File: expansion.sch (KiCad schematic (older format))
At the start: 3 parts, among them J7 DF40HC(3.5)-60DS, J9 DF40HC(3.5)-60DS, U1 IMX8MM

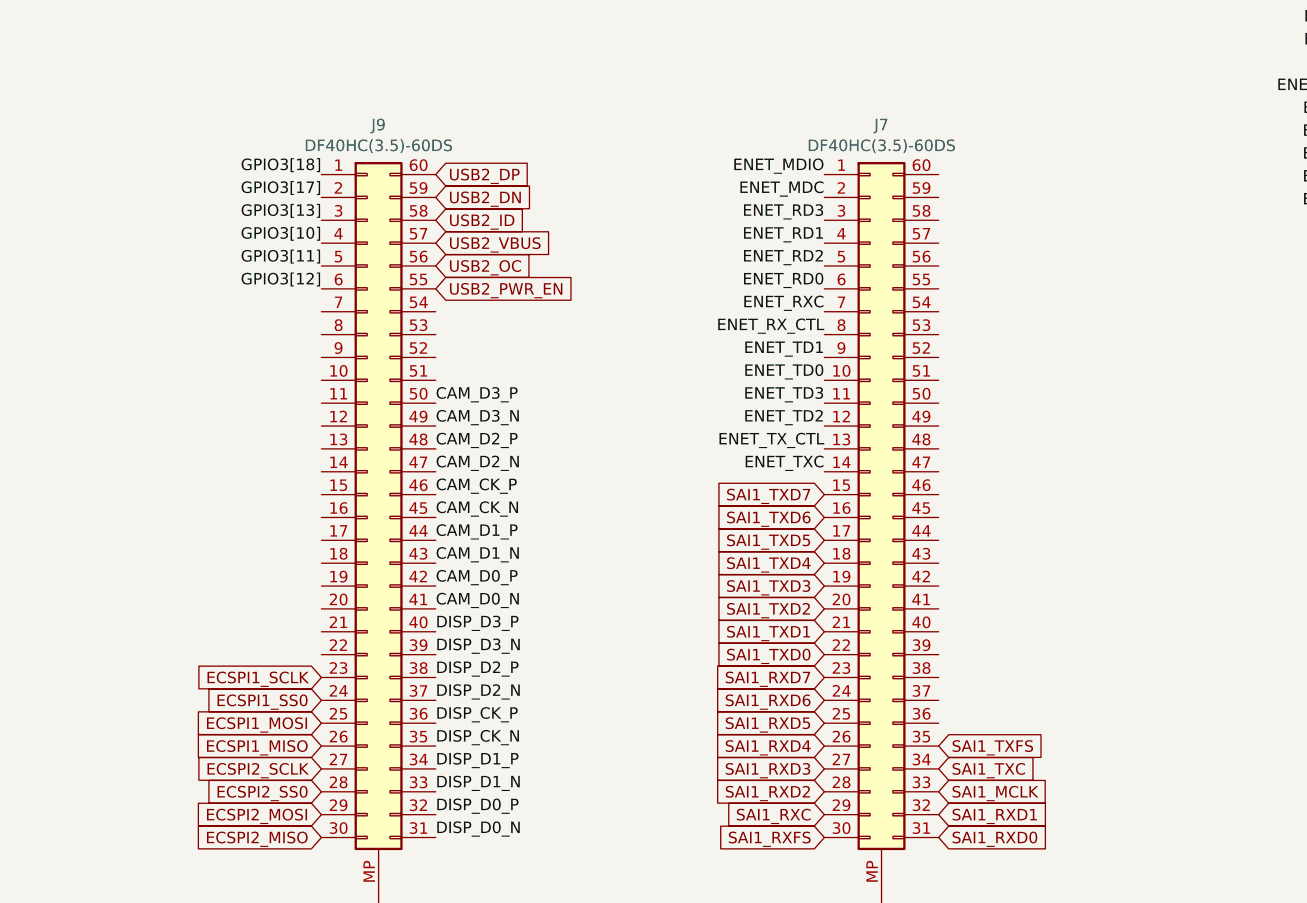
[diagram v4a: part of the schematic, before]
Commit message: UIM and USB routing for PCIE to expansion
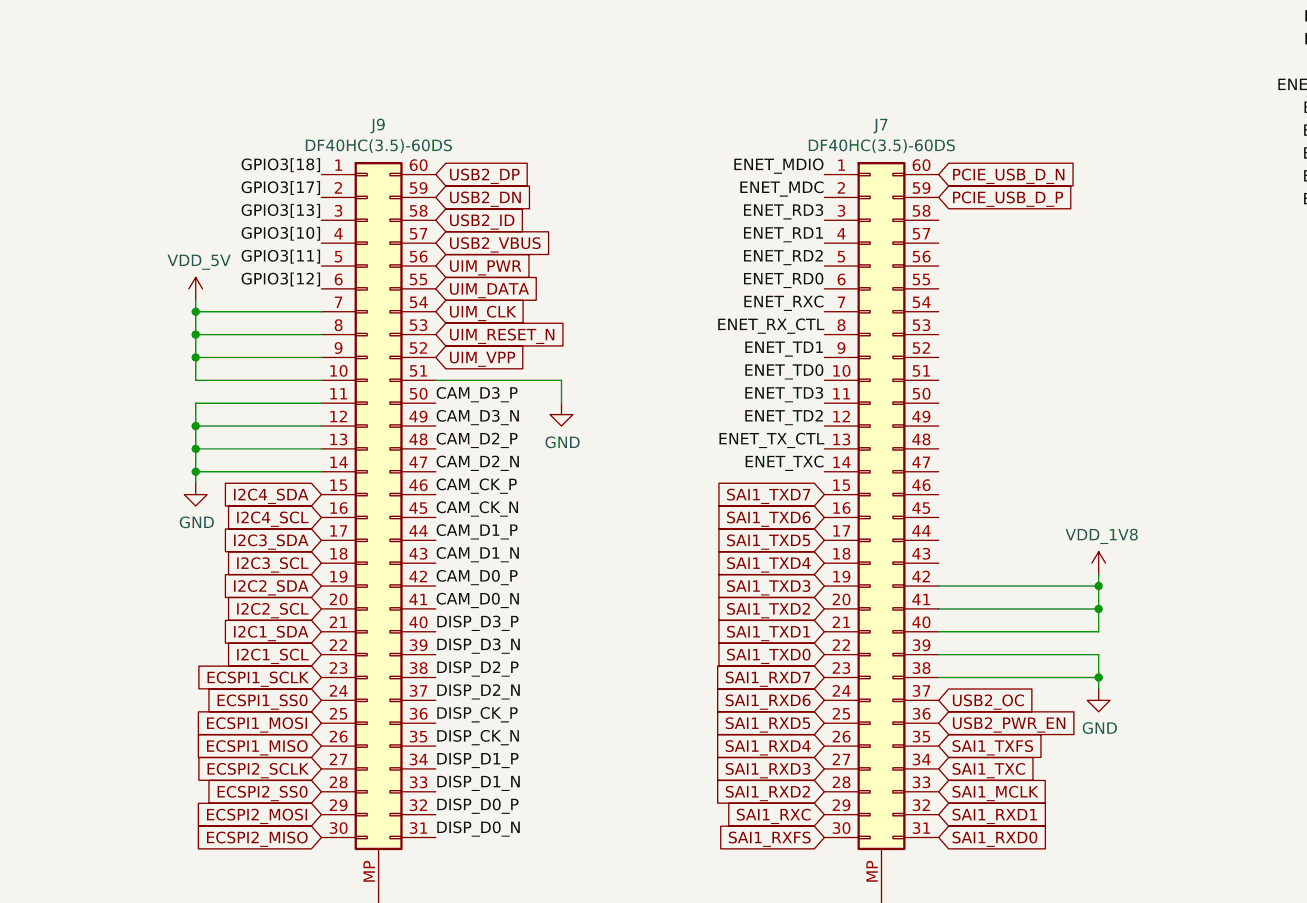
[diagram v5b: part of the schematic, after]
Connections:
- net GND: now also J7.38 (Pin_38), J7.39 (Pin_39), J9.11 (Pin_11), J9.12 (Pin_12), J9.13 (Pin_13), J9.14 (Pin_14), J9.51 (Pin_51)
- net USB2_OC: now also J7.37 (Pin_37); no longer J9.56 (Pin_56)
- net USB2_PWR_EN: now also J7.36 (Pin_36); no longer J9.55 (Pin_55)
- net VDD_5V: now reaches J9.10 (Pin_10)
- net VDD_5V: now also J9.7 (Pin_7), J9.8 (Pin_8), J9.9 (Pin_9)
- net I2C4_SDA: now reaches J9.15 (Pin_15)
- net I2C4_SCL: now reaches J9.16 (Pin_16)
- net I2C3_SDA: now reaches J9.17 (Pin_17)
- net I2C3_SCL: now reaches J9.18 (Pin_18)
- net I2C2_SDA: now reaches J9.19 (Pin_19)
- net I2C2_SCL: now reaches J9.20 (Pin_20)
- net I2C1_SDA: now reaches J9.21 (Pin_21)
- net I2C1_SCL: now reaches J9.22 (Pin_22)
- net UIM_VPP: now reaches J9.52 (Pin_52)
- net UIM_RESET_N: now reaches J9.53 (Pin_53)
- net UIM_CLK: now reaches J9.54 (Pin_54)
- net VDD_1V8: now reaches J7.40 (Pin_40)
- net VDD_1V8: now also J7.41 (Pin_41), J7.42 (Pin_42)
- net PCIE_USB_D_P: now reaches J7.59 (Pin_59)
- net PCIE_USB_D_N: now reaches J7.60 (Pin_60)
- new net UIM_DATA: J9.55 (Pin_55)
- new net UIM_PWR: J9.56 (Pin_56)
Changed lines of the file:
@@
 $Descr A4 11693 8268
 encoding utf-8
-Sheet 10 10
+Sheet 9 10
 Title ""
 Date ""
@@
 Text GLabel 2750 1900 2    50   Input ~ 0
 BTN1
-Text GLabel 5050 2950 2    50   Input ~ 0
+Text GLabel 7250 4850 2    50   Input ~ 0
 USB2_OC
-Text GLabel 5050 3050 2    50   Input ~ 0
+Text GLabel 7250 4950 2    50   Input ~ 0
 USB2_PWR_EN
 Text GLabel 4550 5150 0    50   Input ~ 0
@@
 Text GLabel 4550 4850 0    50   Input ~ 0
 ECSPI1_SS0
+Text GLabel 4550 4650 0    50   Input ~ 0
+I2C1_SCL
+Text GLabel 4550 4550 0    50   Input ~ 0
+I2C1_SDA
+Text GLabel 4550 4350 0    50   Input ~ 0
+I2C2_SDA
+Text GLabel 4550 4150 0    50   Input ~ 0
+I2C3_SDA
+Text GLabel 4550 3950 0    50   Input ~ 0
+I2C4_SDA
+Text GLabel 4550 4450 0    50   Input ~ 0
+I2C2_SCL
+Text GLabel 4550 4250 0    50   Input ~ 0
+I2C3_SCL
+Text GLabel 4550 4050 0    50   Input ~ 0
+I2C4_SCL
+Text GLabel 5050 3250 2    50   Input ~ 0
+UIM_RESET_N
+Text GLabel 5050 3150 2    50   Input ~ 0
+UIM_CLK
+Text GLabel 5050 3050 2    50   Input ~ 0
+UIM_DATA
+Text GLabel 5050 2950 2    50   Input ~ 0
+UIM_PWR
+Text GLabel 5050 3350 2    50   Input ~ 0
+UIM_VPP
+$Comp
+L power:GND #PWR0219
+U 1 1 5F4229EE
+P 5600 3550
+F 0 "#PWR0219" H 5600 3300 50  0001 C CNN
+F 1 "GND" H 5605 3377 50  0000 C CNN
+F 2 "" H 5600 3550 50  0001 C CNN
+F 3 "" H 5600 3550 50  0001 C CNN
+	1    5600 3550
+	1    0    0    -1
+$EndComp
+Wire Wire Line
+	5600 3550 5600 3450
+Wire Wire Line
+	5600 3450 5050 3450
+$Comp
+L mxenc:VDD_5V #PWR0220
+U 1 1 5F42799C
+P 4000 3100
+F 0 "#PWR0220" H 4000 2950 50  0001 C CNN
+F 1 "VDD_5V" H 4015 3273 50  0000 C CNN
+F 2 "" H 4000 3100 50  0001 C CNN
+F 3 "" H 4000 3100 50  0001 C CNN
+	1    4000 3100
+	1    0    0    -1
+$EndComp
+Wire Wire Line
+	4000 3100 4000 3150
+Wire Wire Line
+	4000 3150 4550 3150
+Wire Wire Line
+	4550 3450 4000 3450
+Wire Wire Line
+	4000 3450 4000 3350
+Connection ~ 4000 3150
+Wire Wire Line
+	4550 3350 4000 3350
+Connection ~ 4000 3350
+Wire Wire Line
+	4000 3350 4000 3250
+Wire Wire Line
+	4550 3250 4000 3250
+Connection ~ 4000 3250
+Wire Wire Line
+	4000 3250 4000 3150
+$Comp
+L power:GND #PWR0221
+U 1 1 5F42D118
+P 4000 3900
+F 0 "#PWR0221" H 4000 3650 50  0001 C CNN
+F 1 "GND" H 4005 3727 50  0000 C CNN
+F 2 "" H 4000 3900 50  0001 C CNN
+F 3 "" H 4000 3900 50  0001 C CNN
+	1    4000 3900
+	1    0    0    -1
+$EndComp
+Wire Wire Line
+	4550 3850 4000 3850
+Wire Wire Line
+	4000 3850 4000 3900
+Wire Wire Line
+	4550 3750 4000 3750
+Wire Wire Line
+	4000 3750 4000 3850
+Connection ~ 4000 3850
+Wire Wire Line
+	4550 3650 4000 3650
+Wire Wire Line
+	4000 3650 4000 3750
+Connection ~ 4000 3750
+Wire Wire Line
+	4550 3550 4000 3550
+Wire Wire Line
+	4000 3550 4000 3650
+Connection ~ 4000 3650
+$Comp
+L power:GND #PWR0222
+U 1 1 5F468948
+P 7950 4800
+F 0 "#PWR0222" H 7950 4550 50  0001 C CNN
+F 1 "GND" H 7955 4627 50  0000 C CNN
+F 2 "" H 7950 4800 50  0001 C CNN
+F 3 "" H 7950 4800 50  0001 C CNN
+	1    7950 4800
+	1    0    0    -1
+$EndComp
+Wire Wire Line
+	7950 4800 7950 4750
+Wire Wire Line
+	7950 4750 7250 4750
+Wire Wire Line
+	7250 4650 7950 4650
+Wire Wire Line
+	7950 4650 7950 4750
+Connection ~ 7950 4750
+$Comp
+L mxenc:VDD_1V8 #PWR0223
+U 1 1 5F46F757
+P 7950 4300
+F 0 "#PWR0223" H 7950 4150 50  0001 C CNN
+F 1 "VDD_1V8" H 7965 4473 50  0000 C CNN
+F 2 "" H 7950 4300 50  0001 C CNN
+F 3 "" H 7950 4300 50  0001 C CNN
+	1    7950 4300
+	1    0    0    -1
+$EndComp
+Wire Wire Line
+	7950 4300 7950 4350
+Wire Wire Line
+	7950 4550 7250 4550
+Wire Wire Line
+	7250 4450 7950 4450
+Connection ~ 7950 4450
+Wire Wire Line
+	7950 4450 7950 4550
+Wire Wire Line
+	7950 4350 7250 4350
+Connection ~ 7950 4350
+Wire Wire Line
+	7950 4350 7950 4450
+Text GLabel 7250 2550 2    50   Input ~ 0
+PCIE_USB_D_N
+Text GLabel 7250 2650 2    50   Input ~ 0
+PCIE_USB_D_P
 $EndSCHEMATC

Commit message: Finish remaining routing
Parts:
- added J10: Conn_02x05_Odd_Even, Connector_PinHeader_1.27mm:PinHeader_2x05_P1.27mm_Vertical_SMD, symbol Connector_Generic:Conn_02x05_Odd_Even
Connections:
- net GND: now also J7.43 (Pin_43), J10.3 (Pin_3), J10.5 (Pin_5), J10.9 (Pin_9)
- net JTAG_TCK: now also J10.4 (Pin_4)
- net JTAG_TDI: now also J10.8 (Pin_8)
- net JTAG_TDO: now also J10.6 (Pin_6)
- net JTAG_TMS: now also J10.2 (Pin_2)
- net JTAG_TRST_B: now also J10.10 (Pin_10)
- net VDD_1V8: now also J10.1 (Pin_1)
- net UART1_TX: now reaches J7.44 (Pin_44)
- net UART1_RX: now reaches J7.45 (Pin_45)
- net UART1_CTS_B: now reaches J7.46 (Pin_46)
- net UART1_RTS_B: now reaches J7.47 (Pin_47)
- no-connect marks 0 -> 1
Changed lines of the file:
@@
 	1    0    0    -1
 $EndComp
-Text GLabel 5350 1100 2    50   Input ~ 0
+Text GLabel 4950 1250 2    50   Input ~ 0
 JTAG_TCK
-Text GLabel 5350 1200 2    50   Input ~ 0
+Text GLabel 4950 1150 2    50   Input ~ 0
 JTAG_TMS
-Text GLabel 5350 1300 2    50   Input ~ 0
+Text GLabel 4950 1450 2    50   Input ~ 0
 JTAG_TDI
-Text GLabel 5350 1400 2    50   Input ~ 0
+Text GLabel 4950 1350 2    50   Input ~ 0
 JTAG_TDO
-Text GLabel 5350 1500 2    50   Input ~ 0
+Text GLabel 4950 1550 2    50   Input ~ 0
 JTAG_TRST_B
-Text GLabel 5350 1600 2    50   Input ~ 0
-JTAG_MOD
 $Comp
 L mxenc:MIMX8MM6DVTLZAA U1
@@
 	7950 4750 7250 4750
 Wire Wire Line
-	7250 4650 7950 4650
+	7250 4650 7850 4650
 Wire Wire Line
 	7950 4650 7950 4750
@@
 Text GLabel 7250 2650 2    50   Input ~ 0
 PCIE_USB_D_P
+Text GLabel 7250 3950 2    50   Input ~ 0
+UART1_CTS_B
+Text GLabel 7250 3850 2    50   Input ~ 0
+UART1_RTS_B
+Text GLabel 7250 4050 2    50   Input ~ 0
+UART1_RX
+Text GLabel 7250 4150 2    50   Input ~ 0
+UART1_TX
+Wire Wire Line
+	7250 4250 7850 4250
+Wire Wire Line
+	7850 4250 7850 4650
+Connection ~ 7850 4650
+Wire Wire Line
+	7850 4650 7950 4650
+$Comp
+L Connector_Generic:Conn_02x05_Odd_Even J10
+U 1 1 5EC3A2D4
+P 4650 1350
+F 0 "J10" H 4700 1767 50  0000 C CNN
+F 1 "Conn_02x05_Odd_Even" H 4700 1676 50  0000 C CNN
+F 2 "Connector_PinHeader_1.27mm:PinHeader_2x05_P1.27mm_Vertical_SMD" H 4650 1350 50  0001 C CNN
+F 3 "~" H 4650 1350 50  0001 C CNN
+	1    4650 1350
+	1    0    0    -1
+$EndComp
+$Comp
+L power:GND #PWR0239
+U 1 1 5EC40863
+P 4100 1600
+F 0 "#PWR0239" H 4100 1350 50  0001 C CNN
+F 1 "GND" H 4105 1427 50  0000 C CNN
+F 2 "" H 4100 1600 50  0001 C CNN
+F 3 "" H 4100 1600 50  0001 C CNN
+	1    4100 1600
+	1    0    0    -1
+$EndComp
+Wire Wire Line
+	4100 1600 4100 1550
+Wire Wire Line
+	4100 1350 4450 1350
+Wire Wire Line
+	4450 1250 4100 1250
+Wire Wire Line
+	4100 1250 4100 1350
+Connection ~ 4100 1350
+Wire Wire Line
+	4450 1550 4100 1550
+Connection ~ 4100 1550
+Wire Wire Line
+	4100 1550 4100 1350
+NoConn ~ 4450 1450
+$Comp
+L mxenc:VDD_1V8 #PWR0244
+U 1 1 5ED1315B
+P 4100 950
+F 0 "#PWR0244" H 4100 800 50  0001 C CNN
+F 1 "VDD_1V8" H 4115 1123 50  0000 C CNN
+F 2 "" H 4100 950 50  0001 C CNN
+F 3 "" H 4100 950 50  0001 C CNN
+	1    4100 950
+	1    0    0    -1
+$EndComp
+Wire Wire Line
+	4100 950  4100 1150
+Wire Wire Line
+	4100 1150 4450 1150
 $EndSCHEMATC

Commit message: wip more uart routing
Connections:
- net USB2_OC is gone; now on net SAI1_MCLK: J7.37 (Pin_37)
- net USB2_PWR_EN is gone; now on net SAI1_RXD1: J7.36 (Pin_36)
- net GND: no longer J7.38 (Pin_38), J7.39 (Pin_39), J7.43 (Pin_43)
- net SAI1_MCLK: no longer J7.33 (Pin_33)
- net SAI1_RXD0: now also J7.35 (Pin_35); no longer J7.31 (Pin_31)
- net SAI1_RXD1: no longer J7.32 (Pin_32)
- net SAI1_TXC: now also J7.38 (Pin_38); no longer J7.34 (Pin_34)
- net SAI1_TXFS: now also J7.39 (Pin_39); no longer J7.35 (Pin_35)
- net UART3_TX: now reaches J7.48 (Pin_48)
- net UART3_RX: now reaches J7.49 (Pin_49)
- net UART1_CTS_B: no longer names the net of J7.46 (Pin_46)
- net UART1_RTS_B: no longer names the net of J7.47 (Pin_47)
- new net GPIO1[11]: J7.34 (Pin_34)
- new net GPIO1[14]: J7.32 (Pin_32)
- new net GPIO1[15]: J7.33 (Pin_33)
- new net GPIO1[9]: J7.31 (Pin_31)
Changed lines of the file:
@@
 Text GLabel 6750 5450 0    50   Input ~ 0
 SAI1_RXFS
-Text GLabel 7250 5350 2    50   Input ~ 0
+Text GLabel 7250 4950 2    50   Input ~ 0
 SAI1_RXD1
-Text GLabel 7250 5450 2    50   Input ~ 0
+Text GLabel 7250 5050 2    50   Input ~ 0
 SAI1_RXD0
-Text GLabel 7250 5150 2    50   Input ~ 0
+Text GLabel 7250 4750 2    50   Input ~ 0
 SAI1_TXC
-Text GLabel 7250 5050 2    50   Input ~ 0
+Text GLabel 7250 4650 2    50   Input ~ 0
 SAI1_TXFS
-Text GLabel 7250 5250 2    50   Input ~ 0
+Text GLabel 7250 4850 2    50   Input ~ 0
 SAI1_MCLK
 Text Label 2750 2800 0    50   ~ 0
@@
 Text GLabel 2750 1900 2    50   Input ~ 0
 BTN1
-Text GLabel 7250 4850 2    50   Input ~ 0
-USB2_OC
-Text GLabel 7250 4950 2    50   Input ~ 0
-USB2_PWR_EN
 Text GLabel 4550 5150 0    50   Input ~ 0
 ECSPI2_SCLK
@@
 Connection ~ 4000 3650
 $Comp
-L power:GND #PWR0222
-U 1 1 5F468948
-P 7950 4800
-F 0 "#PWR0222" H 7950 4550 50  0001 C CNN
-F 1 "GND" H 7955 4627 50  0000 C CNN
-F 2 "" H 7950 4800 50  0001 C CNN
-F 3 "" H 7950 4800 50  0001 C CNN
-	1    7950 4800
-	1    0    0    -1
-$EndComp
-Wire Wire Line
-	7950 4800 7950 4750
-Wire Wire Line
-	7950 4750 7250 4750
-Wire Wire Line
-	7250 4650 7850 4650
-Wire Wire Line
-	7950 4650 7950 4750
-Connection ~ 7950 4750
-$Comp
 L mxenc:VDD_1V8 #PWR0223
 U 1 1 5F46F757
@@
 Text GLabel 7250 2650 2    50   Input ~ 0
 PCIE_USB_D_P
-Text GLabel 7250 3950 2    50   Input ~ 0
-UART1_CTS_B
-Text GLabel 7250 3850 2    50   Input ~ 0
-UART1_RTS_B
+Text GLabel 7250 3750 2    50   Input ~ 0
+UART3_TX
+Text GLabel 7250 3650 2    50   Input ~ 0
+UART3_RX
 Text GLabel 7250 4050 2    50   Input ~ 0
 UART1_RX
 Text GLabel 7250 4150 2    50   Input ~ 0
 UART1_TX
-Wire Wire Line
-	7250 4250 7850 4250
-Wire Wire Line
-	7850 4250 7850 4650
-Connection ~ 7850 4650
-Wire Wire Line
-	7850 4650 7950 4650
 $Comp
 L Connector_Generic:Conn_02x05_Odd_Even J10
@@
 Wire Wire Line
 	4100 1150 4450 1150
+Text GLabel 7250 5450 2    50   Input ~ 0
+GPIO1[9]
+Text GLabel 7250 5150 2    50   Input ~ 0
+GPIO1[11]
+Text GLabel 7250 5350 2    50   Input ~ 0
+GPIO1[14]
+Text GLabel 7250 5250 2    50   Input ~ 0
+GPIO1[15]
 $EndSCHEMATC
